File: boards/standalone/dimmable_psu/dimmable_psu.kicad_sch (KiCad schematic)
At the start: 1 part, among them U1 TPS92640

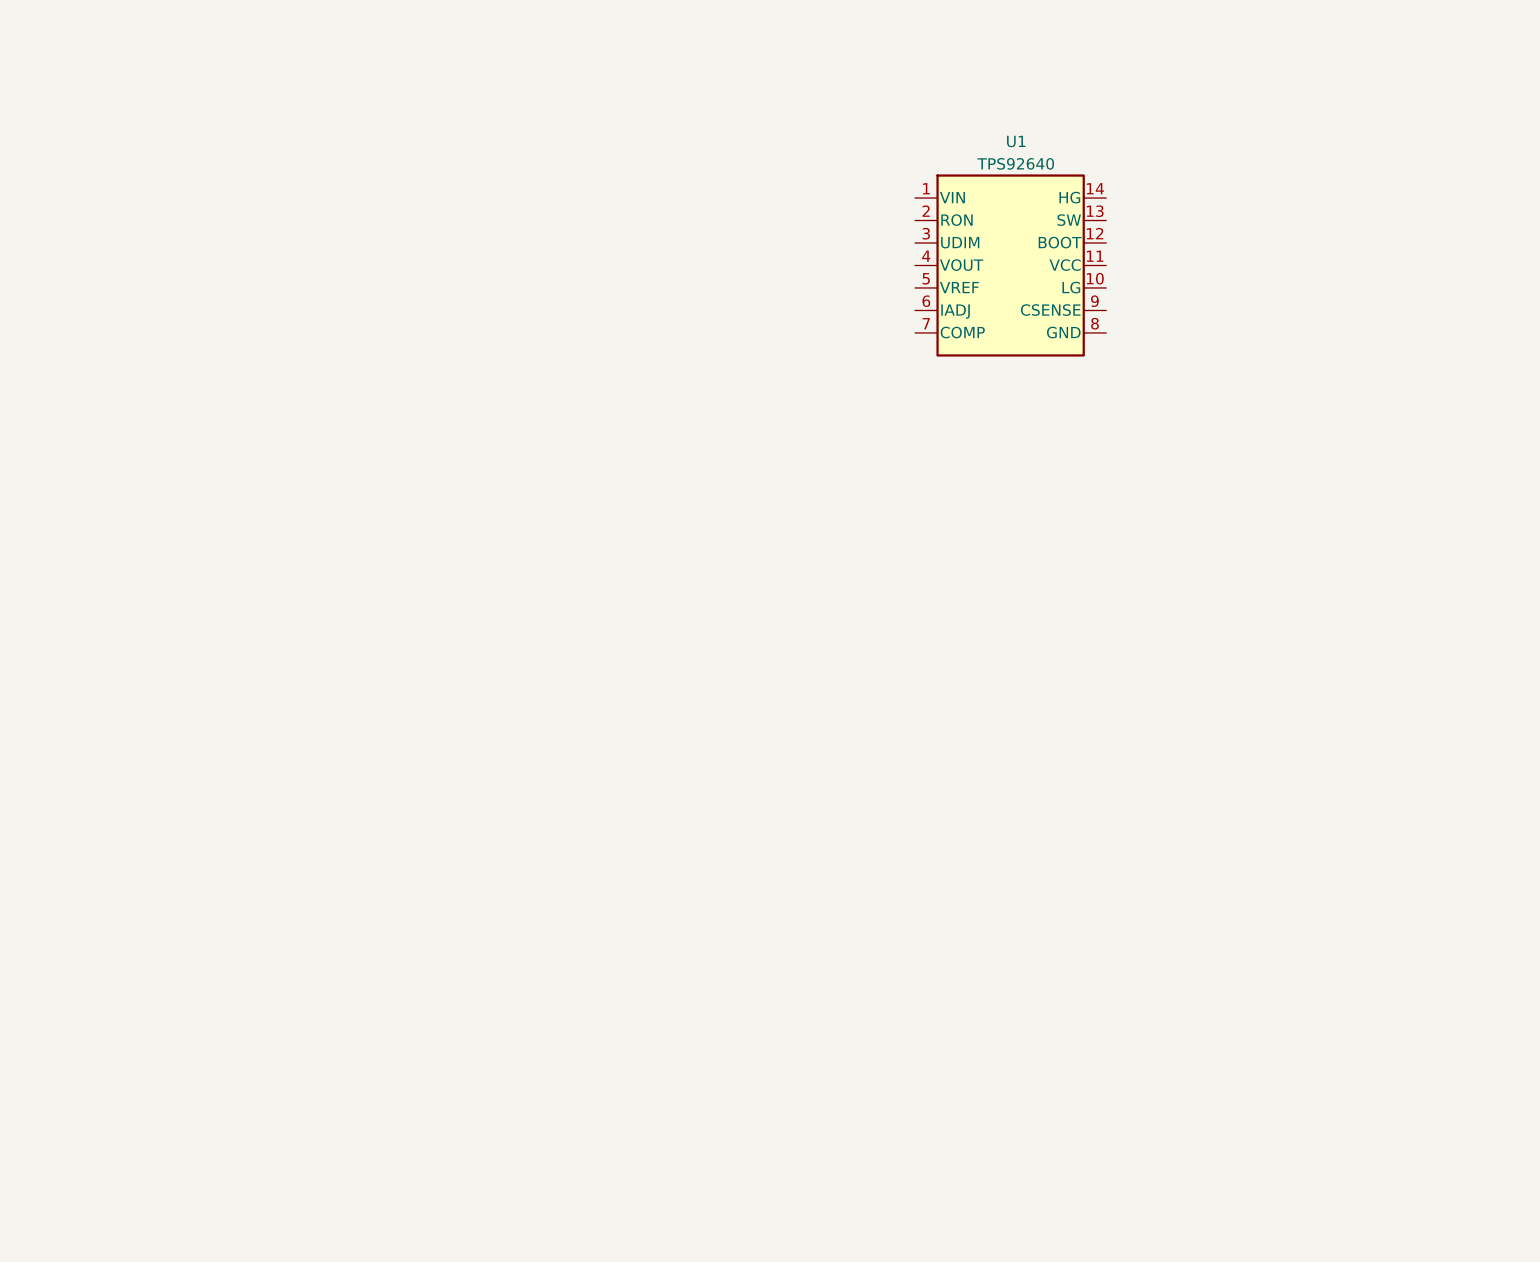
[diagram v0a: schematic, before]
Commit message: current adjustment reference voltage generator
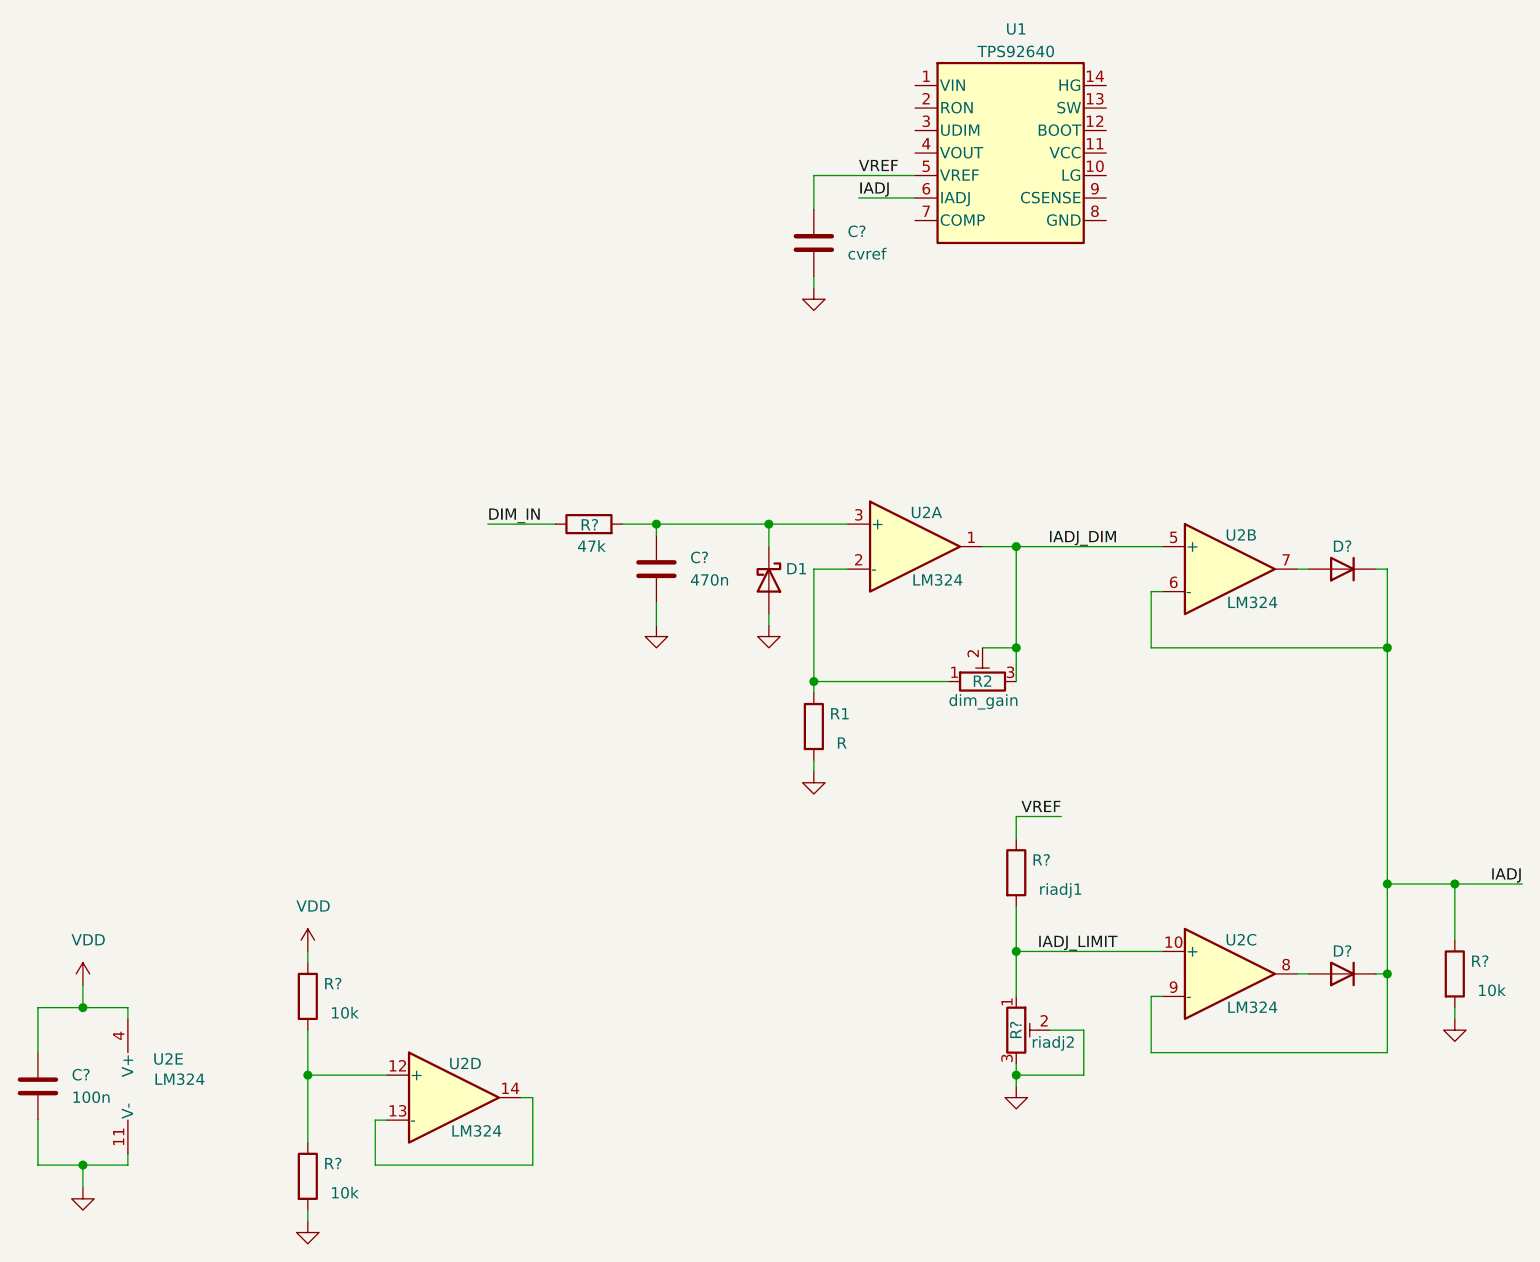
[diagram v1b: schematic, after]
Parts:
- added C?: cvref, Capacitor_SMD:C_0805_2012Metric_Pad1.18x1.45mm_HandSolder, symbol Device:C
- added C?: 100n, Capacitor_SMD:C_0805_2012Metric_Pad1.18x1.45mm_HandSolder, symbol Device:C
- added C?: 470n, Capacitor_SMD:C_0805_2012Metric_Pad1.18x1.45mm_HandSolder, symbol Device:C
- added D1: D_Schottky, symbol Device:D_Schottky
- added D? (x2): D, Diode_SMD:D_SOD-123, symbol Device:D
- added R1: R, Resistor_SMD:R_0805_2012Metric_Pad1.20x1.40mm_HandSolder, symbol Device:R
- added R2: dim_gain, symbol Device:R_Potentiometer_Trim
- added R? (x3): 10k, Resistor_SMD:R_0805_2012Metric_Pad1.20x1.40mm_HandSolder, symbol Device:R
- added R?: riadj2, symbol Device:R_Potentiometer_Trim
- added R?: 47k, Resistor_SMD:R_0805_2012Metric_Pad1.20x1.40mm_HandSolder, symbol Device:R
- added R?: riadj1, Resistor_SMD:R_0805_2012Metric_Pad1.20x1.40mm_HandSolder, symbol Device:R
- added U2: LM324, Package_SO:SO-14_3.9x8.65mm_P1.27mm, symbol Amplifier_Operational:LM324
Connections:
- net VREF: now reaches U1.5 (VREF)
- net VREF: now also C?.1, R?.1
- net IADJ: now reaches U1.6 (IADJ)
- net IADJ: now also D?.1 (K), D?.1 (K), R?.1, U2.6 (-), U2.9 (-)
- new net: R?.1, R?.2, U2.12 (+)
- new net: U2.13 (-), U2.14
- new net: R1.1, R2.1, U2.2 (-)
- new net: D?.2 (A), U2.7
- new net: D?.2 (A), U2.8
- new net: C?.1, D1.1 (K), R?.2, U2.3 (+)
- new net DIM_IN: R?.1
- new net GND: C?.2, C?.2, C?.2, D1.2 (A), R1.2, R?.2, R?.2, R?.2, R?.3, U2.11 (V-)
- new net IADJ_DIM: R2.2, R2.3, U2.1, U2.5 (+)
- new net IADJ_LIMIT: R?.1, R?.2, U2.10 (+)
- new net VDD: C?.1, R?.1, U2.4 (V+)
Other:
- title: (none) -> dimmable_psu
- moved on the sheet: U1

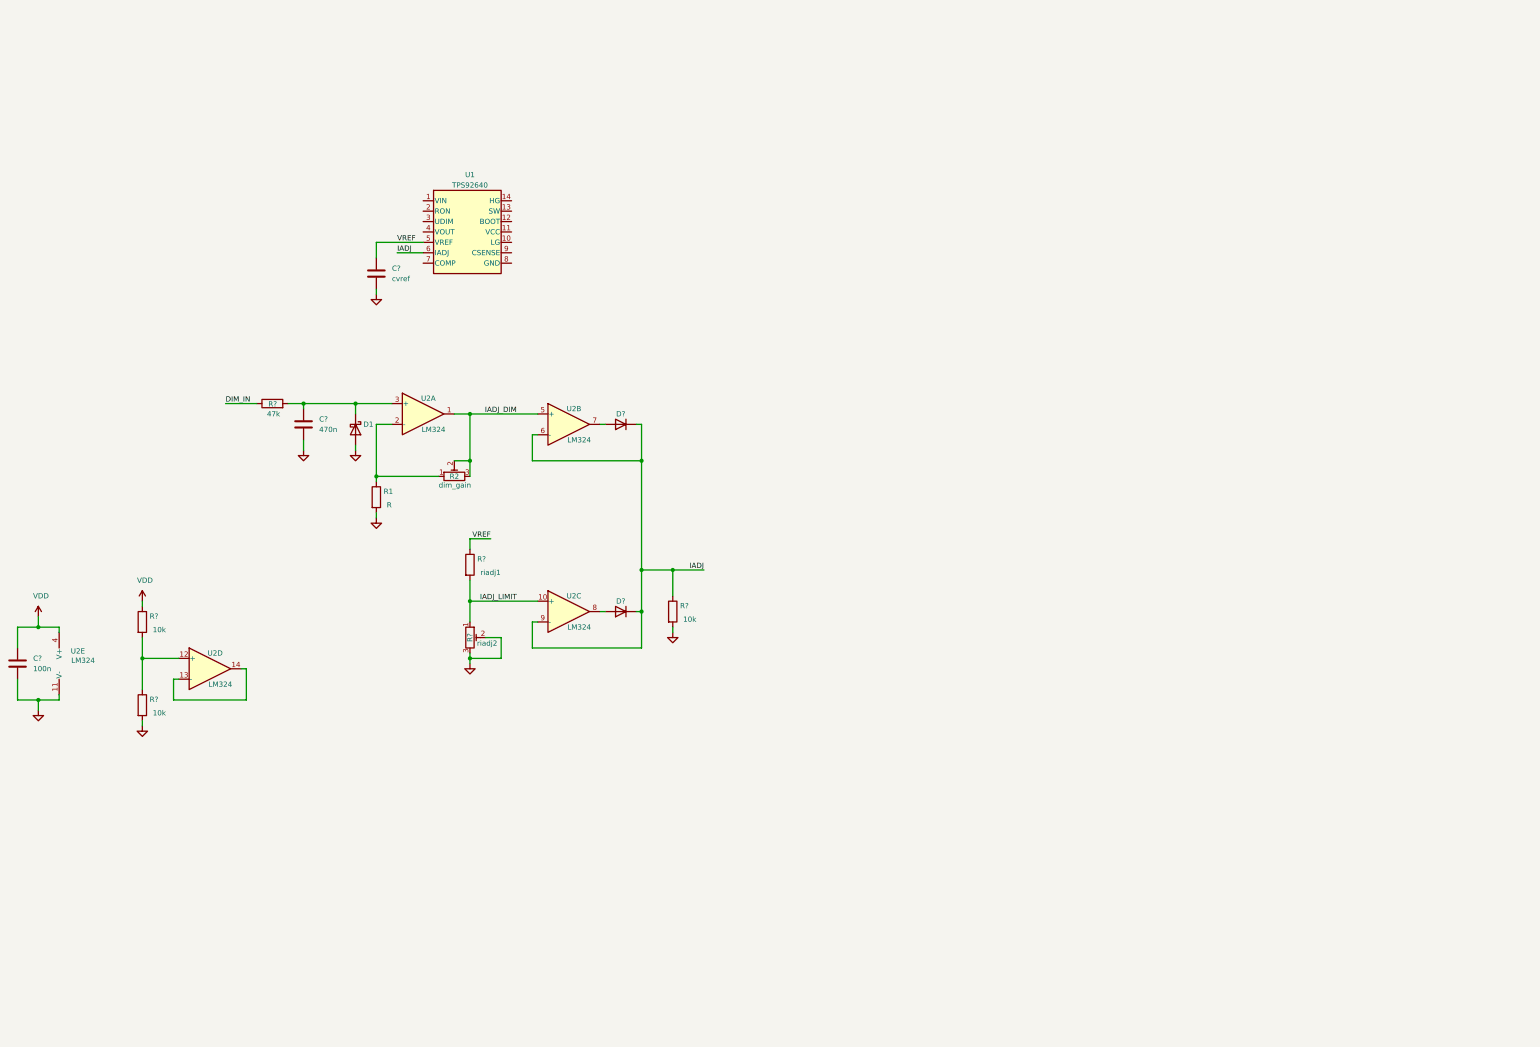
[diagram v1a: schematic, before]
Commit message: analog logic for dimming and clamping
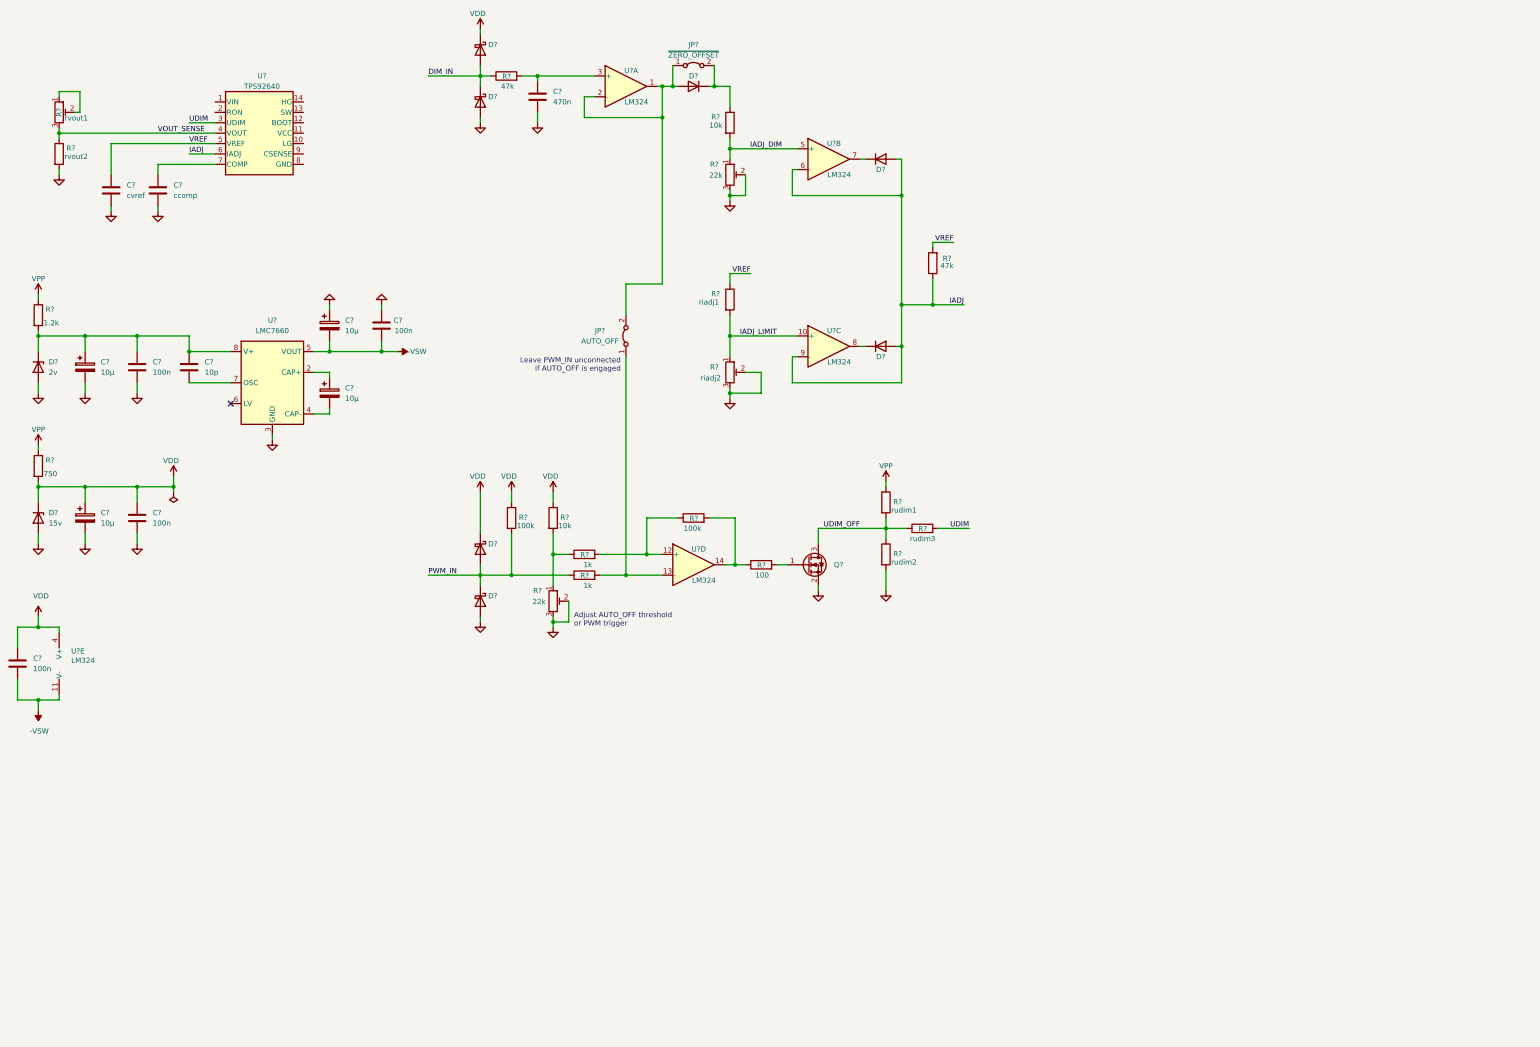
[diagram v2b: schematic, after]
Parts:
- removed D1: D_Schottky, symbol Device:D_Schottky
- removed R1: R, Resistor_SMD:R_0805_2012Metric_Pad1.20x1.40mm_HandSolder, symbol Device:R
- removed R?: 10k, Resistor_SMD:R_0805_2012Metric_Pad1.20x1.40mm_HandSolder, symbol Device:R
- added C? (x4): 10µ, symbol Device:C_Polarized
- added C?: 10p, Capacitor_SMD:C_0805_2012Metric_Pad1.18x1.45mm_HandSolder, symbol Device:C
- added C? (x3): 100n, Capacitor_SMD:C_0805_2012Metric_Pad1.18x1.45mm_HandSolder, symbol Device:C
- added C?: ccomp, Capacitor_SMD:C_0805_2012Metric_Pad1.18x1.45mm_HandSolder, symbol Device:C
- added D?: 15v, Diode_SMD:D_SOD-123, symbol Device:D_Zener
- added D? (x4): D_Schottky, symbol Device:D_Schottky
- added D?: D, Diode_SMD:D_SOD-123, symbol Device:D
- added D?: 2v, Diode_SMD:D_SOD-123, symbol Device:D_Zener
- added JP?: ~ZERO_OFFSET, symbol Jumper:Jumper_2_Bridged
- added JP?: AUTO_OFF, symbol Jumper:Jumper_2_Bridged
- added Q?: 2N7002, Package_TO_SOT_SMD:SOT-23, symbol Transistor_FET:2N7002
- added R?: rvout2, Resistor_SMD:R_0805_2012Metric_Pad1.20x1.40mm_HandSolder, symbol Device:R
- added R?: 10k, Resistor_SMD:R_0805_2012Metric_Pad1.20x1.40mm_HandSolder, symbol Device:R
- added R? (x2): 100k, Resistor_SMD:R_0805_2012Metric_Pad1.20x1.40mm_HandSolder, symbol Device:R
- added R?: rudim2, Resistor_SMD:R_0805_2012Metric_Pad1.20x1.40mm_HandSolder, symbol Device:R
- added R? (x2): 1k, Resistor_SMD:R_0805_2012Metric_Pad1.20x1.40mm_HandSolder, symbol Device:R
- added R?: rudim1, Resistor_SMD:R_0805_2012Metric_Pad1.20x1.40mm_HandSolder, symbol Device:R
- added R?: 1.2k, Resistor_SMD:R_0805_2012Metric_Pad1.20x1.40mm_HandSolder, symbol Device:R
- added R?: 22k, Potentiometer_THT:Potentiometer_Bourns_3296Y_Vertical, symbol Device:R_Potentiometer_Trim
- added R?: 100, Resistor_SMD:R_0805_2012Metric_Pad1.20x1.40mm_HandSolder, symbol Device:R
- added R?: rvout1, Potentiometer_THT:Potentiometer_Bourns_3296Y_Vertical, symbol Device:R_Potentiometer_Trim
- added R?: rudim3, Resistor_SMD:R_0805_2012Metric_Pad1.20x1.40mm_HandSolder, symbol Device:R
- added R?: 750, Resistor_SMD:R_0805_2012Metric_Pad1.20x1.40mm_HandSolder, symbol Device:R
- added U?: LMC7660, symbol Regulator_SwitchedCapacitor:LMC7660
- R?: renamed from R2; value dim_gain -> 22k; footprint (none) -> Potentiometer_THT:Potentiometer_Bourns_3296Y_Vertical
- R?: footprint (none) -> Potentiometer_THT:Potentiometer_Bourns_3296Y_Vertical
- R?: value 10k -> 47k
- renumbered U2 to U?, U1 to U?
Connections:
- net DIM_IN: now also D?.1 (K), D?.2 (A)
- net GND: now also R?.2, R?.3, C?.1, C?.2, C?.2, C?.2, C?.2, C?.2, C?.2, D?.2 (A), D?.2 (A), D?.2 (A), D?.2 (A), Q?.2 (S), R?.2, R?.2, R?.2, R?.3, U?.3 (GND); no longer C?.2, R?.2, U?.11 (V-)
- net IADJ: now also D?.2 (A), D?.2 (A); no longer D?.1 (K), D?.1 (K)
- net IADJ_DIM: now also R?.1, R?.2; no longer R?.2, R?.3, U?.1
- net VDD: now also C?.1, C?.1, D?.1 (K), D?.1 (K), D?.1 (K), R?.1, R?.2
- net VREF: now also R?.2
- net at R?.2: now also R?.1, R?.1; no longer U?.12 (+)
- net at U?.13 (-): now also JP?.1 (A), R?.2; no longer U?.14
- net at U?.2 (-): now also U?.1, D?.2 (A), JP?.1 (A), JP?.2 (B); no longer R?.1
- net UDIM: now reaches U?.3 (UDIM)
- net UDIM: now also R?.2
- net VOUT_SENSE: now reaches U?.4 (VOUT)
- net VOUT_SENSE: now also R?.1, R?.3
- net at U?.7 (COMP): now also C?.1
- net at U?.7: now also D?.1 (K); no longer D?.2 (A)
- net at U?.8: now also D?.1 (K); no longer D?.2 (A)
- new net: C?.1, C?.1, C?.1, D?.1 (K), R?.2, U?.8 (V+)
- new net: C?.1, U?.2 (CAP+)
- new net: C?.2, U?.4 (CAP-)
- new net: C?.2, U?.7 (OSC)
- new net: R?.1, R?.2, U?.12 (+)
- new net: R?.1, R?.2, U?.14
- new net: Q?.1 (G), R?.2
- new net: D?.1 (K), JP?.2 (B), R?.1
- new net: R?.1, R?.2
- new net -VSW: C?.1, C?.2, C?.2, U?.11 (V-), U?.5 (VOUT)
- new net PWM_IN: D?.1 (K), D?.2 (A), R?.1, R?.2
- new net UDIM_OFF: Q?.3 (D), R?.1, R?.1, R?.2
- new net VPP: R?.1, R?.1, R?.1
- no-connect marks 0 -> 1
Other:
- note added: "Adjust AUTO_OFF threshold or PWM trigger"
- note added: "Leave PWM_IN unconnected if AUTO_OFF is engaged"
- moved on the sheet: C?, D?, R?, U?, U?A, U?B, U?C, U?D
